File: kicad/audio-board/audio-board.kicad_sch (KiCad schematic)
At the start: 45 parts, among them J1 TO_CM5, J2 VBAT_IN, U1 ADAU1861, U10 ADP7118AUJZ-3.3-R7, U2 ADXL354CEZ, U3 LTC6242, U4 IM72D128VV01, U5 AD2428WBCPZ, U6 SN74LVC8T245PWR, U7 SN74LVC8T245PWR, U8 PCA9517ADP, U9 ADP7118AUJZ-1.8-R7

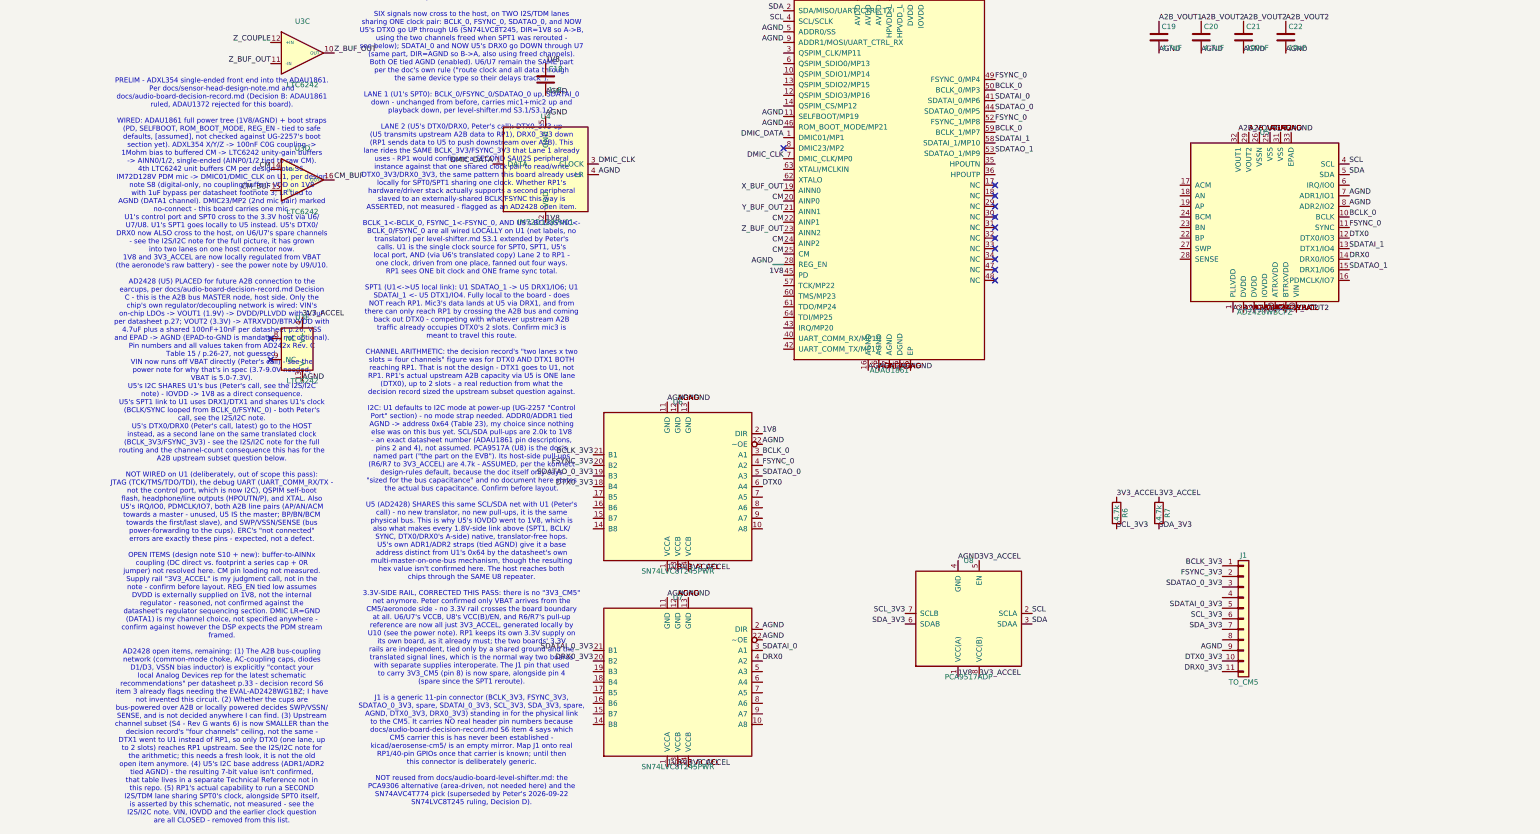
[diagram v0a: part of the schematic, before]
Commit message: [LIMA] wire the AD2428 A2B bus-coupling network (B-side) from ADI's own master-node eval board
The datasheet itself withholds this circuit: AD242x Rev. C p.33 says to "contact your local Analog
Devices representative for the latest schematic circuit recommendations... required for A2B
automotive-grade compliance." Rather than invent it or guess from generic differential-pair
practice, found and transcribed the real thing: EVAL-AD2428WD1BZ, ADI's own A2B MASTER-node eval
board (matches Decision C - this board's U5 is also a master), schematic Rev 1.1, sheet 2 of 7.
analog.com blocks curl/WebFetch at the connection level as usual; fetched by hand through a real
browser, archived at docs/datasheets/EVAL-AD2428WD1BZ_schematics.pdf, checksum-pinned in
fetch-datasheets.sh.

Wired FB1/FB2 (1000R ferrite beads BP/BN to BCM), C27 (12pF across the pair), L1/L2 (180nH series),
C28 (27pF to AGND), FL1 (2600R common-mode choke), R8/R9 (120R split termination) with C29 (centre
tap to AGND), C30/C31 (0.01uF AC coupling), C32/C33/C34 (line-side caps), L3/L4 (3.3uH DC bias
injection), and J3 (placeholder 2-pin connector to the cups) - every value read directly off the
eval board drawing, not guessed. L4 -> U5 VSSN per the datasheet's own Table 15 (negative bias
inductor). A-side (AP/AN/ACM) stays unconnected on purpose: U5 is the master, nothing sits upstream.

Two things flagged, not silently resolved: (1) A2B_BIAS_P has no source - the eval board's
bus-power switch (Q1, D4/D5/D9, the SENSE divider) wasn't copied, because it only makes sense once
the bus-powered-vs-locally-powered decision for the cups is made, and the master needs bias for
line diagnostics either way this comes out. (2) An eval board is not ADI's issued recommendation -
that distinction is called out explicitly, on the schematic and in the new
docs/a2b-bus-coupling-note.md, as needing review with ADI before fab.

Full transcription table, what was deliberately not copied, and the mandatory AD242x p.34 layout
rules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
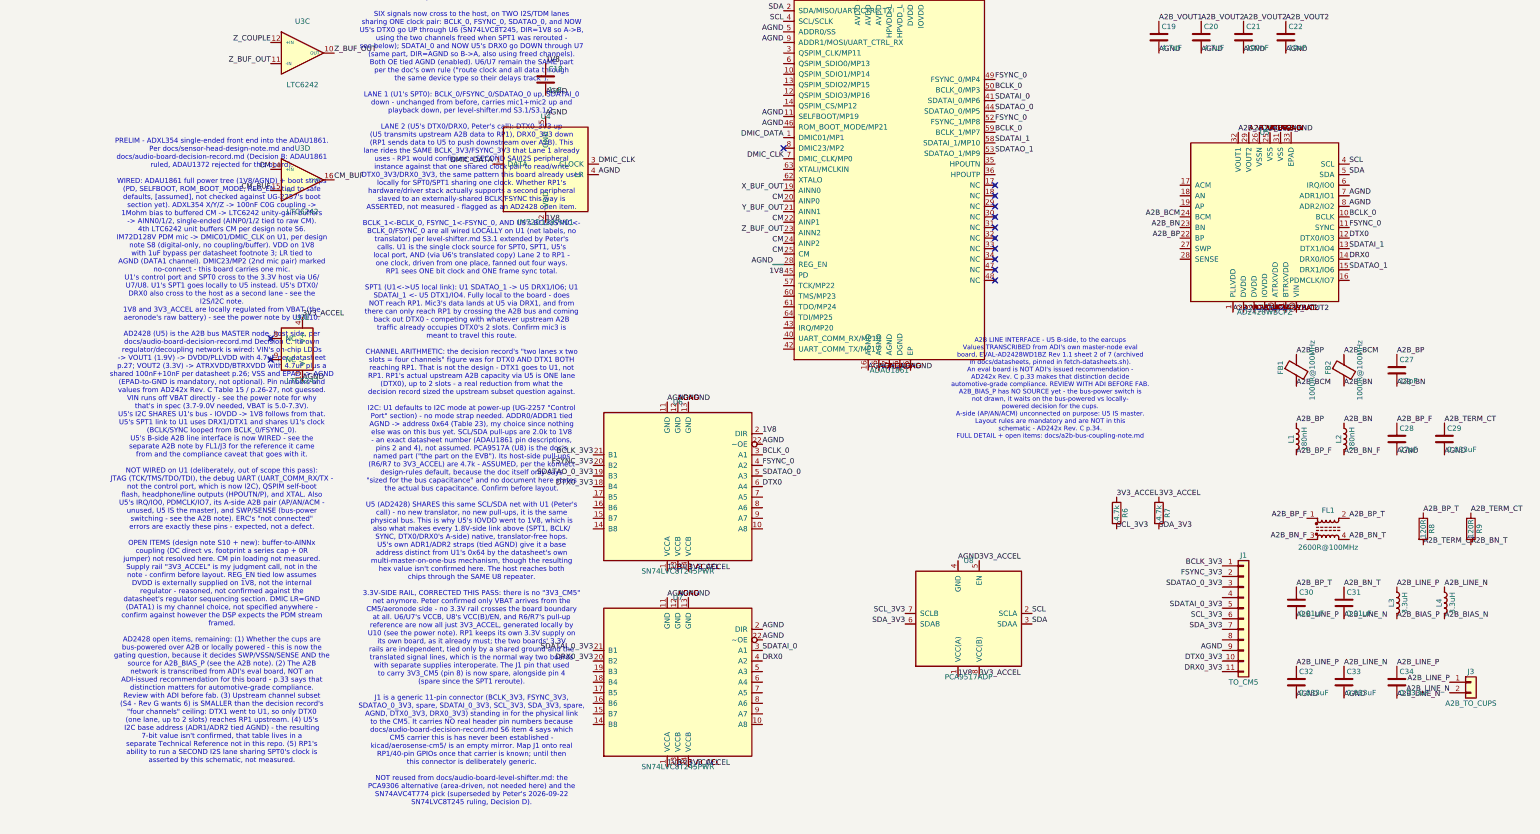
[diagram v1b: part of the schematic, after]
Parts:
- added C27: 12pF, symbol Device:C
- added C28: 27pF, symbol Device:C
- added C29, C32, C33, C34: 0.033uF, symbol Device:C
- added C30, C31: 0.01uF, symbol Device:C
- added FB1, FB2: 1000R@100MHz, symbol Device:FerriteBead
- added FL1: 2600R@100MHz, symbol Filter:Choke_CommonMode_FerriteCore_1234
- added J3: A2B_TO_CUPS, symbol Connector_Generic:Conn_01x02
- added L1, L2: 180nH, symbol Device:L
- added L3, L4: 3.3uH, symbol Device:L
- added R8, R9: 120R, symbol Device:R
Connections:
- net AGND: now also C28.2, C29.2, C32.2, C33.2
- net A2B_BP: now reaches U5.22 (BP)
- net A2B_BP: now also C27.1, FB1.1, L1.1
- net A2B_BN: now reaches U5.23 (BN)
- net A2B_BN: now also C27.2, FB2.2, L2.1
- net A2B_BCM: now reaches U5.24 (BCM)
- net A2B_BCM: now also FB1.2, FB2.1
- net A2B_BIAS_N: now reaches U5.26 (VSSN)
- net A2B_BIAS_N: now also L4.2
- new net A2B_BIAS_P: L3.2
- new net A2B_BN_F: FL1.3, L2.2
- new net A2B_BN_T: C31.1, FL1.4, R9.2
- new net A2B_BP_F: C28.1, FL1.1, L1.2
- new net A2B_BP_T: C30.1, FL1.2, R8.1
- new net A2B_LINE_N: C31.2, C33.1, C34.2, J3.2 (Pin_2), L4.1
- new net A2B_LINE_P: C30.2, C32.1, C34.1, J3.1 (Pin_1), L3.1
- new net A2B_TERM_CT: C29.1, R8.2, R9.1
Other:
- note added: "A2B LINE INTERFACE - U5 B-side, to the earcups Values TRANSCRIBED from ADI's own master-node eval board, EVAL-AD2428WD1BZ Rev 1.1 sheet 2 of 7 (archived in docs/datasheets, pinned in fetch-datasheets.sh). An eval board is NOT ADI's issued recommendation - AD242x Rev. C p.33 makes that distinction decide automotive-grade compliance. REVIEW WITH ADI BEFORE FAB. A2B_BIAS_P has NO SOURCE yet - the bu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"

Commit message: [LIMA] add sheet 2: relay switches aircraft mic jack between ADAU1861 out and boom mic, per Peter
New hierarchical sheet "BOOM MIC / TX SELECT" (page 2): K1 (G6K-2F-Y,
same qualified relay as the H1 headset-mute board) switches what
reaches a new 3.5mm TRS jack (-> PJ068 aircraft adapter, per Peter)
between ADAU1861's HPOUTP (previously unwired) and a new boom-mic-
from-earcup connector. De-energized defaults to the boom mic path
(pilot's mic survives a power/control loss) - flagged on the sheet
for confirmation, not yet ruled. Standard low-side coil driver
(2N7002 + flyback diode + gate pulldown) from a new GPIO on J1 pin 4
(previously spare). HPOUTN left no-connect, same treatment as HPOUTN
on the H1 board.

Caught and fixed a real short during routing: the coil-return wire
and the switched-audio wire were briefly collinear, merging the two
nets. KiCad's ERC (no_connect_connected) caught it; rerouted with
non-overlapping doglegs.

Verified: ERC 49->46 errors (exactly the 3 newly-connected pins),
0 shorted nets, 0 overlaps, both sheets rendered and checked.

Open, flagged in the schematic text: relay coil supply has no source
(G6K-2F-Y needs 5V, VBAT is 5.0-7.3V); HPOUTP has no blocking-cap/
clamp protection against aircraft mic bias; TRS Ring bias pass-
through undesigned; Sleeve grounds straight to this board's AGND
with no aircraft-side isolation; J4/J5 are generic placeholders
pending the real connector choice.

Co-Authored-By: Claude Sonnet 5 <noreply@anthropic.com>
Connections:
- net GPIO_RLY_TX_SEL_3V3: now reaches J1.4 (Pin_4)
- net HPOUTP: now reaches U1.36 (HPOUTP)
- no-connect marks 14 -> 15
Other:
- added sheet BOOM MIC / TX SELECT (boom-mic-tx-select.kicad_sch)
- note added: "HPOUTN intentionally left no-connect: HPOUTP now feeds the new BOOM MIC / TX SELECT sheet (page 2) single-ended. Differential pair, other leg left open not grounded - same treatment as the H1 headset-mute board's HPOUTN. J1 pin 4 (previously spare) now carries GPIO_RLY_TX_SEL_3V3 to that sheet's relay driver."

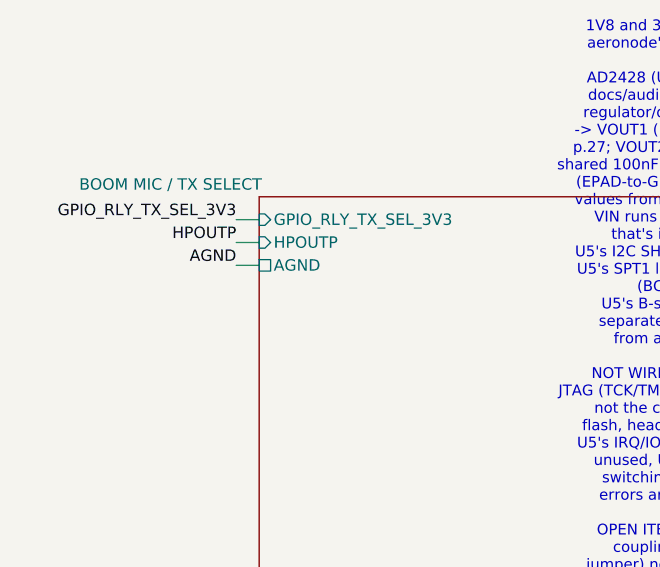
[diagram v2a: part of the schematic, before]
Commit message: [LIMA] resolve relay coil supply: U11 regulates VBAT to 4.5V, per Peter's option 1
Fetched Omron's G6K datasheet (not cached anywhere in this repo before
now) to settle the open item from the previous commit. Checked all five
stock G6K-2F-Y coil options (3/4.5/5/12/24 VDC) against VBAT's 5.0-7.3V
swing: none spans it cleanly for continuous duty. The 5V coil is the
only contender, but VBAT_max (146% of rated) sits right at a rating the
datasheet explicitly says is instantaneous-only, not continuous.

Peter ruled option 1 of 4 (dedicated regulator, vs. a PWM coil
economiser / different relay / borrowing a 5V rail from aeronode).

Added U11 - the SAME ADP7118AUJZ-1.8-R7 already used twice on this
board as U9/U10, wired in its adjustable configuration (R11 15k / R12
10k per the datasheet's own Fig. 39 formula) instead of the fixed
pass-through, to produce a 4.5V RLY_COIL_SUPPLY rail: safely above the
5V coil's 80%-of-rated guaranteed-operate floor, and independent of
VBAT's swing entirely. New VBAT sheet pin added to carry the supply in.

Caught two more of the same collinear-wire short bug this sheet's
initial relay routing hit: the VOUT-to-divider and SENSE/ADJ-to-divider
runs both crossed straight through other pins on their way to R11/R12
because the auto-router's L-path shared a column with the divider
stack. Both rerouted with dogleg paths after ERC/find_shorted_nets
caught them.

Also caught and fixed a real legibility bug in the design-note text
objects: they're center-anchored on both axes (not top-left as
assumed), so the first draft's note ran off the child sheet's edges
and overlapped its own components. Bumped the child sheet to A3 (was
undersized A4 for this much documentation) and repositioned.

Verified: ERC errors unchanged at 46 (no new unconnected pins), 0
shorted nets, 0 overlaps across both sheets, rendered and visually
checked.

Co-Authored-By: Claude Sonnet 5 <noreply@anthropic.com>
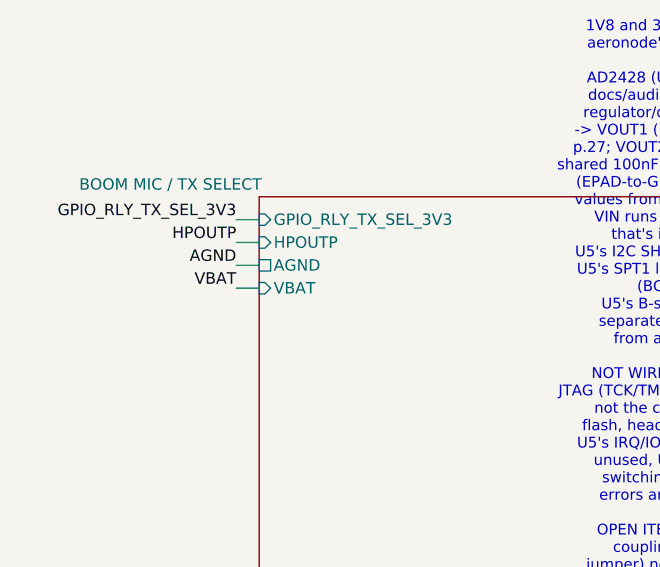
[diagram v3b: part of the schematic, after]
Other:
- sheet BOOM MIC / TX SELECT ports: added VBAT; removed none
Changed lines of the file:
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@@
+		)
+	)
+	(wire
+		(pts
+			(xy 40 210.16)
+			(xy 37.46 210.16)
 		)
 	)
@@
 	(label "AGND"
 		(at 37.46 207.62 180)
+		(effects
+			(font
+				(size 1.27 1.27)
+			)
+			(justify right bottom)
+		)
+	)
+	(label "VBAT"
+		(at 37.46 210.16 180)
 		(effects
 			(font
@@
 			(at 40 207.62 180)
 		)
+		(pin "VBAT" input
+			(at 40 210.16 180)
+		)
 		(instances

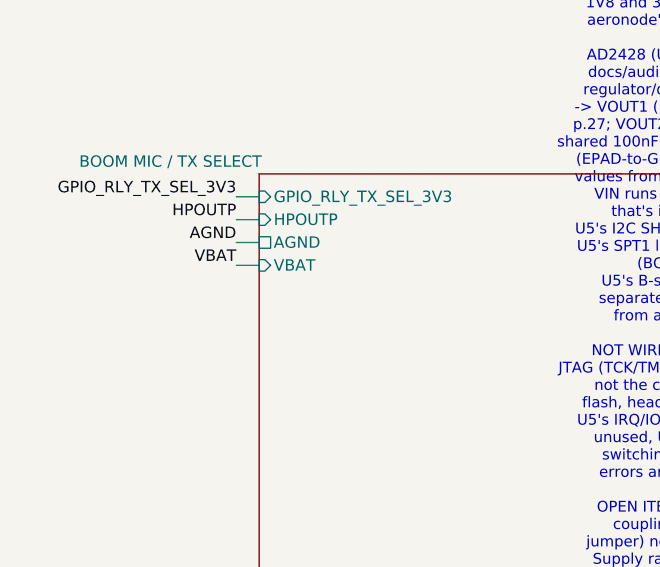
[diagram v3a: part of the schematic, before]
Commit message: [LIMA] add HPOUTP blocking cap + BAT54S clamp, same topology as the H1 board
Resolves the second open item from the previous commit. HPOUTP now
runs through C37 (220nF, C0G/film - not X7R, whose DC-bias derating
would walk the corner into the voice band) then R13 (10k) before
reaching the relay's NO_A contact, with D2 (BAT54S) clamping that
node between AGND and 1V8. Reused the H1 headset-mute board's mic-
line injection topology (its section 10.1) rather than re-deriving
it: R13 after C37 so a shorted cap can't pass more than a resistor-
limited fault current, same reasoning as that board's R1.

Clamp rails are 1V8/AGND specifically because that tracks the
ADAU1861's own abs-max spec ("Analog Input Voltage (Signal Pins)
-0.3V to AVDD+0.3V") rather than an arbitrary value - if AVDD ever
changes, the clamp tracks it by construction. New 1V8 sheet pin
added to carry the rail in from the main sheet's U9 output.

Caught and fixed a label-crowding legibility issue: the new D2/AGND
net label and the pre-existing J5/AGND label were both pointing
toward each other on the same row and overlapping in the render.
Moved one further out.

Verified: ERC errors unchanged at 46, 0 shorted nets, 0 overlaps,
rendered and visually checked.

Co-Authored-By: Claude Sonnet 5 <noreply@anthropic.com>
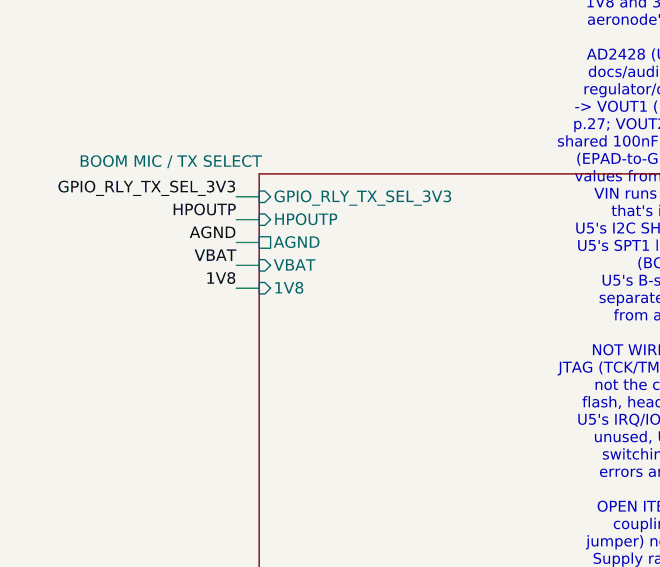
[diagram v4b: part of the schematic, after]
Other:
- sheet BOOM MIC / TX SELECT ports: added 1V8; removed none
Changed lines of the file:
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@@
+		)
+	)
+	(wire
+		(pts
+			(xy 40 212.7)
+			(xy 37.46 212.7)
 		)
 	)
@@
 	(label "VBAT"
 		(at 37.46 210.16 180)
+		(effects
+			(font
+				(size 1.27 1.27)
+			)
+			(justify right bottom)
+		)
+	)
+	(label "1V8"
+		(at 37.46 212.7 180)
 		(effects
 			(font
@@
 			(at 40 210.16 180)
 		)
+		(pin "1V8" input
+			(at 40 212.7 180)
+		)
 		(instances
